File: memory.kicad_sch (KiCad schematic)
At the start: 4 parts

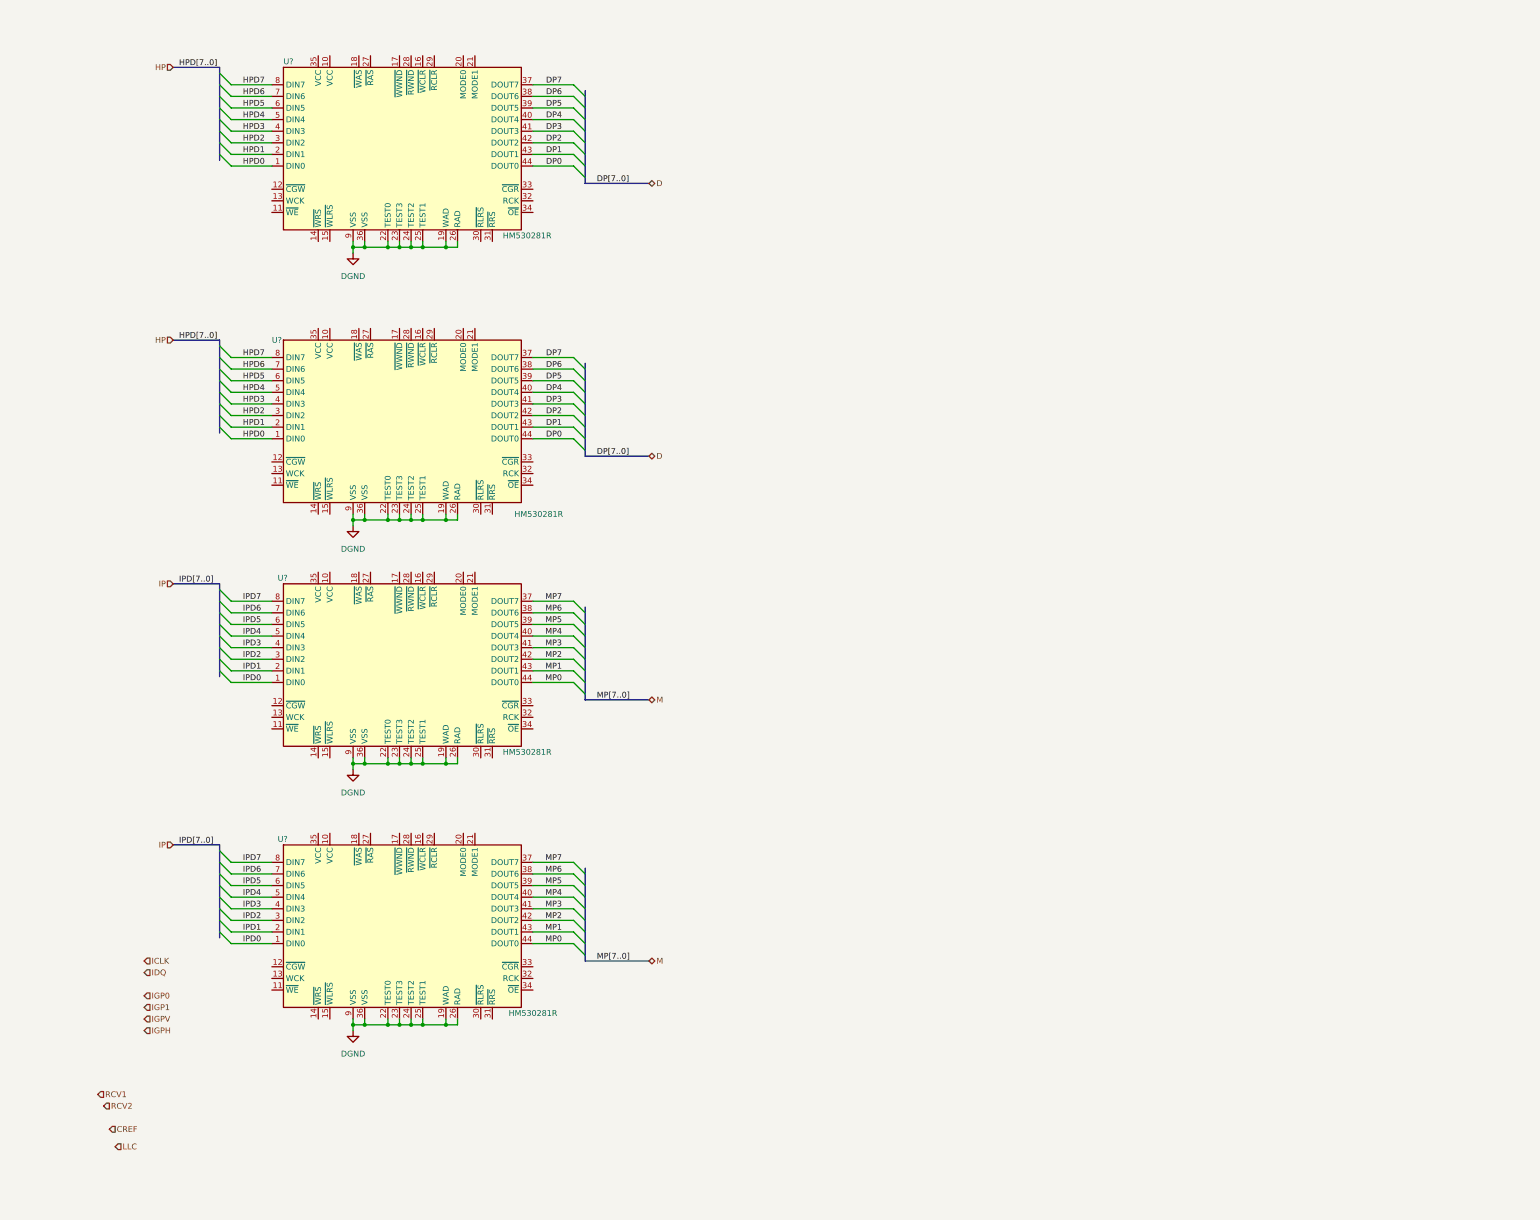
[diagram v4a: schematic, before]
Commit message: continued on schematic, added power sheet
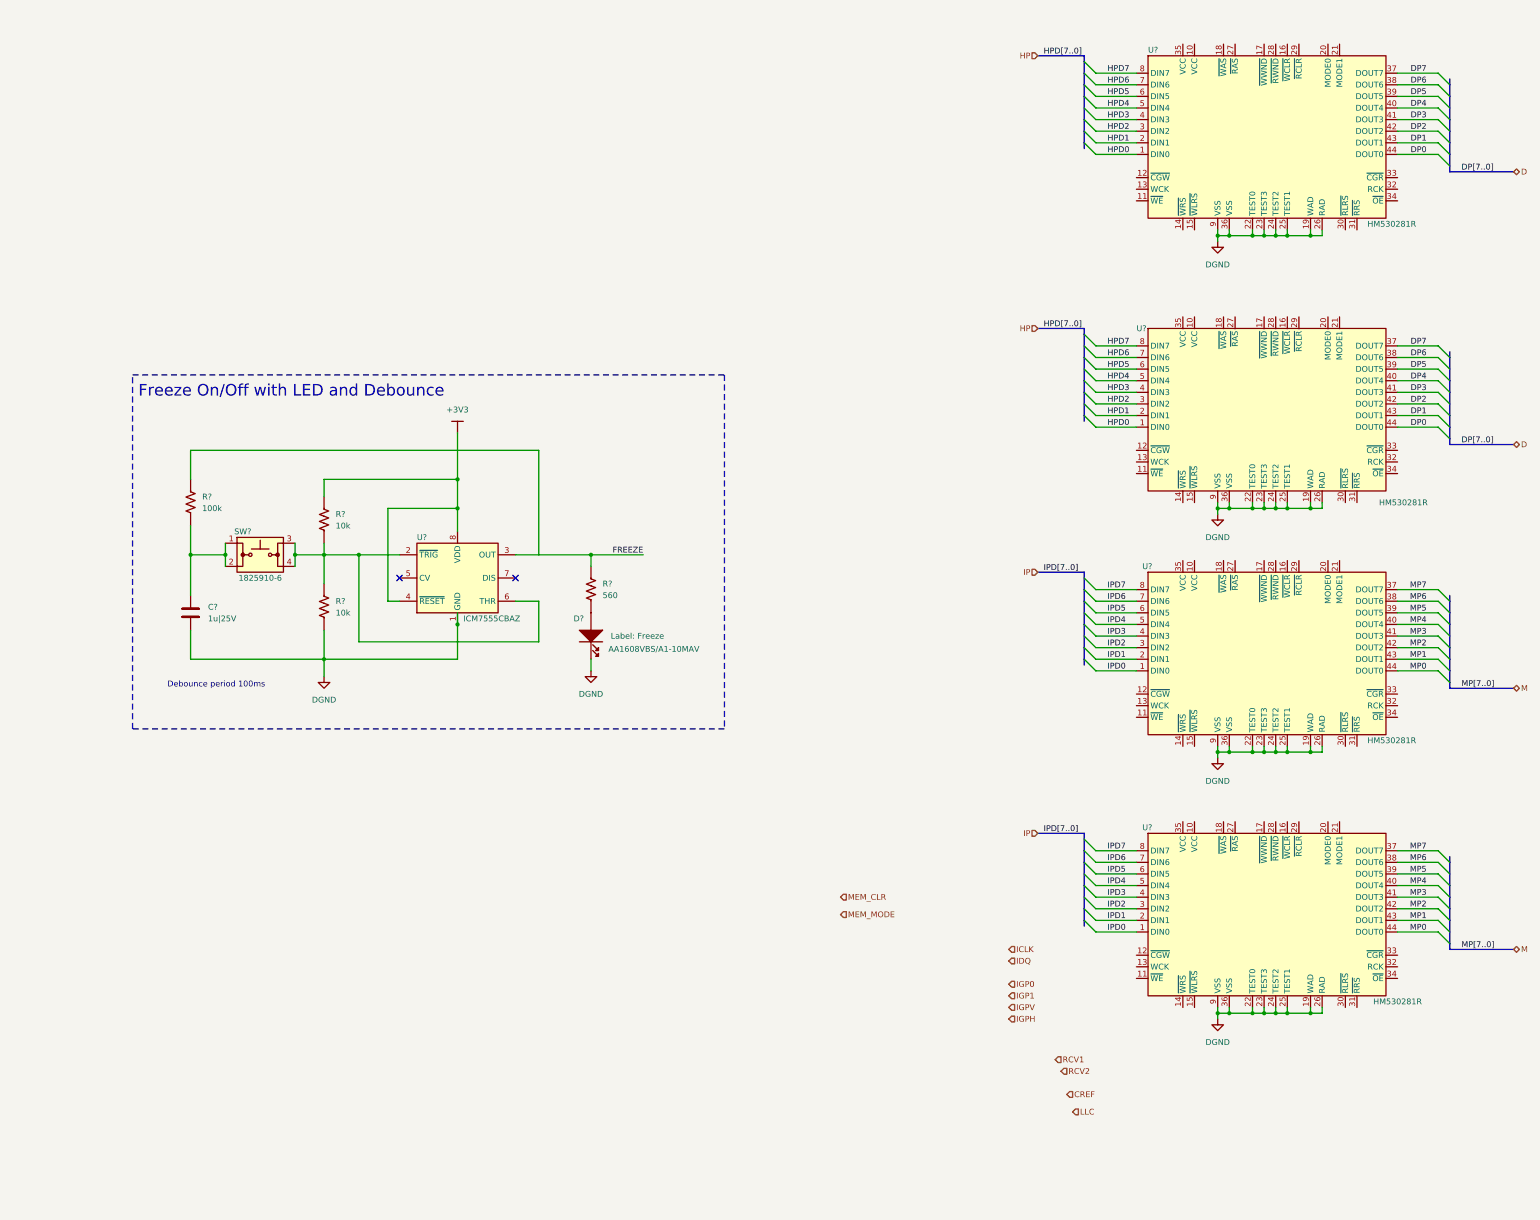
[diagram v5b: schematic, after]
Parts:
- added C?: 1u|25V, symbol tbc:GCJ188R71E105KA01D
- added D?: AA1608VBS/A1-10MAV, symbol tbc:AA1608VBS/A1-10MAV
- added R? (x2): 10k, symbol tbc:RC0603FR-0710KL
- added R?: 560, symbol tbc:RC0603FR-07560RL
- added R?: 100k, symbol tbc:RC0603FR-07100KL
- added SW?: 1825910-6, symbol tbc:1825910-6
- added U?: ICM7555CBAZ, symbol tbc:ICM7555CBAZ
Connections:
- net DGND: now also C?.1, D?.1 (Cathode), R?.1, U?.1 (GND)
- new net: C?.2, R?.1, SW?.1, SW?.2
- new net: R?.1, R?.2, SW?.3, SW?.4, U?.2 (~{TRIG}), U?.6 (THR)
- new net: D?.2 (Anode), R?.1
- new net +3V3: R?.2, U?.4 (~{RESET}), U?.8 (VDD)
- new net FREEZE: R?.2, U?.3 (OUT)
- no-connect marks 0 -> 2
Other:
- note added: "Debounce period 100ms"
- note added: "Freeze On/Off with LED and Debounce"
- moved on the sheet: U?

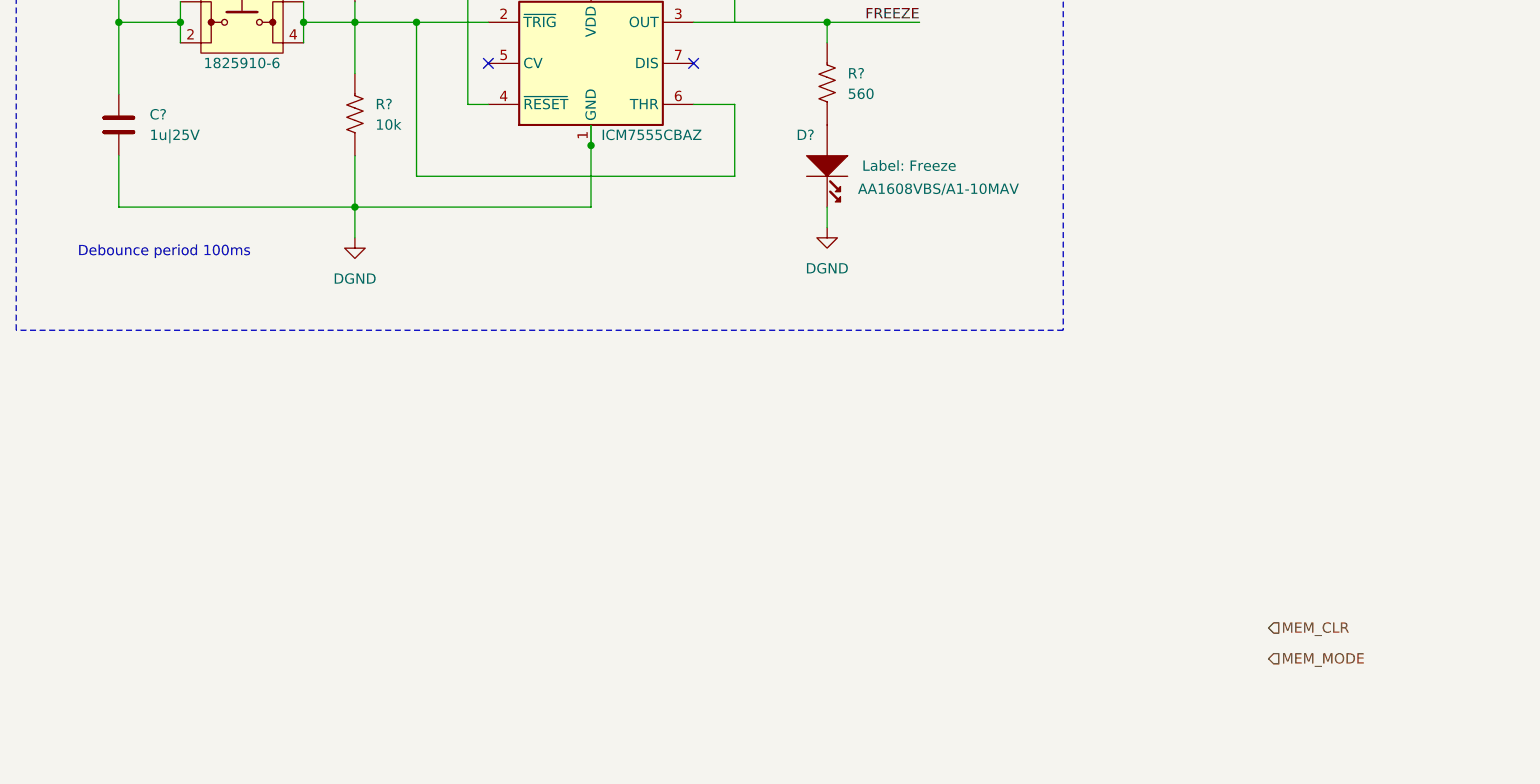
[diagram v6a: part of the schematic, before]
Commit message: added encoder to schematic
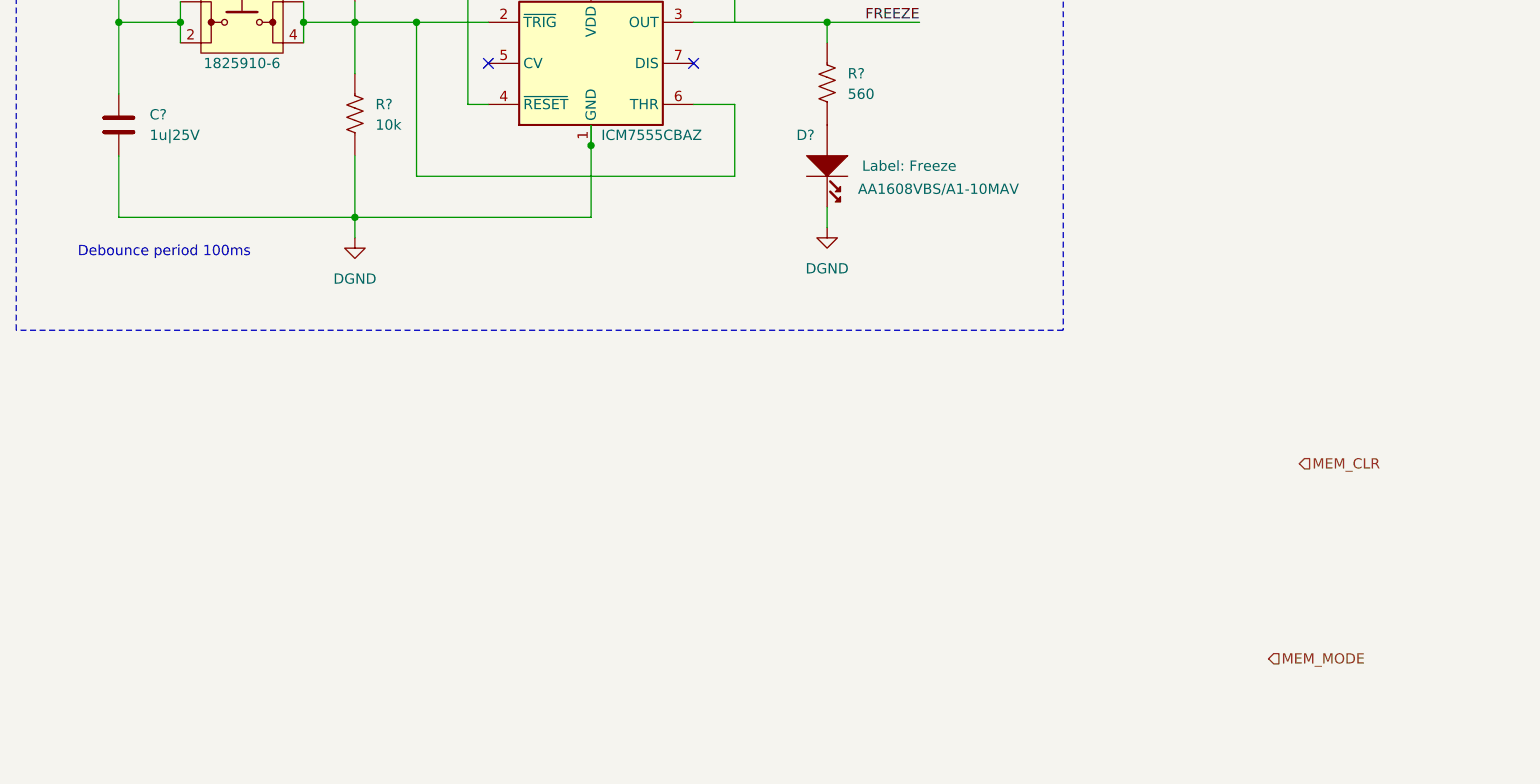
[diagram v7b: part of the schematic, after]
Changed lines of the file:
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@@
   (junction (at 281.94 181.61) (diameter 0) (color 0 0 0 0)
   )
+  (junction (at 83.82 162.56) (diameter 0) (color 0 0 0 0)
+  )
   (junction (at 292.1 238.76) (diameter 0) (color 0 0 0 0)
   )
@@
   )
   (junction (at 289.56 238.76) (diameter 0) (color 0 0 0 0)
-  )
-  (junction (at 83.82 161.29) (diameter 0) (color 0 0 0 0)
   )
   (junction (at 54.61 138.43) (diameter 0) (color 0 0 0 0)
@@
     (stroke (width 0) (type default))
   )
-  (wire (pts (xy 83.82 161.29) (xy 54.61 161.29))
+  (wire (pts (xy 83.82 162.56) (xy 54.61 162.56))
     (stroke (width 0) (type default))
   )
@@
     (stroke (width 0) (type default))
   )
-  (wire (pts (xy 113.03 153.67) (xy 113.03 161.29))
+  (wire (pts (xy 113.03 153.67) (xy 113.03 162.56))
     (stroke (width 0) (type default))
   )
@@
     (stroke (width 0) (type default))
   )
-  (wire (pts (xy 54.61 154.94) (xy 54.61 161.29))
+  (wire (pts (xy 54.61 154.94) (xy 54.61 162.56))
     (stroke (width 0) (type default))
   )
@@
     (stroke (width 0) (type default))
   )
-  (wire (pts (xy 83.82 161.29) (xy 83.82 165.1))
-    (stroke (width 0) (type default))
-  )
   (wire (pts (xy 289.56 68.58) (xy 292.1 68.58))
     (stroke (width 0) (type default))
@@
     (stroke (width 0) (type default))
   )
-  (wire (pts (xy 83.82 161.29) (xy 113.03 161.29))
+  (wire (pts (xy 83.82 162.56) (xy 113.03 162.56))
     (stroke (width 0) (type default))
   )
@@
     (stroke (width 0) (type default))
   )
+  (wire (pts (xy 83.82 162.56) (xy 83.82 165.1))
+    (stroke (width 0) (type default))
+  )
   (wire (pts (xy 289.56 127) (xy 289.56 128.27))
     (stroke (width 0) (type default))
@@
     (stroke (width 0) (type default))
   )
+  (wire (pts (xy 83.82 154.94) (xy 83.82 162.56))
+    (stroke (width 0) (type default))
+  )
   (bus (pts (xy 250.19 199.39) (xy 250.19 200.66))
     (stroke (width 0) (type default))
@@
   )
   (wire (pts (xy 130.81 115.57) (xy 54.61 115.57))
-    (stroke (width 0) (type default))
-  )
-  (wire (pts (xy 83.82 154.94) (xy 83.82 161.29))
     (stroke (width 0) (type default))
   )
@@
     (effects (font (size 1.27 1.27)) (justify right bottom))
   )
-  (hierarchical_label "MEM_CLR" (shape input) (at 196.85 213.36 0) (fields_autoplaced)
+  (hierarchical_label "MEM_CLR" (shape input) (at 200.66 193.04 0) (fields_autoplaced)
     (effects (font (size 1.27 1.27)) (justify left))
   )

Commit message: major progress with memory interfacing
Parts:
- removed C?: 1u|25V, symbol tbc:GCJ188R71E105KA01D
- removed D?: AA1608VBS/A1-10MAV, symbol tbc:AA1608VBS/A1-10MAV
- removed R? (x2): 10k, symbol tbc:RC0603FR-0710KL
- removed R?: 560, symbol tbc:RC0603FR-07560RL
- removed R?: 100k, symbol tbc:RC0603FR-07100KL
- removed SW?: 1825910-6, symbol tbc:1825910-6
- removed U?: ICM7555CBAZ, symbol tbc:ICM7555CBAZ
- added C? (x5): 100n, symbol tbc:GCJ188R71H104KA12D
- added R?: 2K2, symbol tbc:RC0603FR-072K2L
- added R?: 10k, symbol tbc:RC0603FR-0710KL
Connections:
- net DGND is gone; now on net GND: U?.19 (WAD), U?.19 (WAD), U?.19 (WAD), U?.19 (WAD), U?.22 (TEST0), U?.22 (TEST0), U?.22 (TEST0), U?.22 (TEST0), U?.23 (TEST3), U?.23 (TEST3), U?.23 (TEST3), U?.23 (TEST3), U?.24 (TEST2), U?.24 (TEST2), U?.24 (TEST2), U?.24 (TEST2), U?.25 (TEST1), U?.25 (TEST1), U?.25 (TEST1), U?.25 (TEST1), U?.26 (RAD), U?.26 (RAD), U?.26 (RAD), U?.26 (RAD), U?.36 (VSS), U?.36 (VSS), U?.36 (VSS), U?.36 (VSS), U?.9 (VSS), U?.9 (VSS), U?.9 (VSS), U?.9 (VSS)
- net CREF: now also U?.33 (~{CGR}), U?.33 (~{CGR}), U?.33 (~{CGR}), U?.33 (~{CGR})
- net ICLK: now also U?.13 (WCK), U?.13 (WCK), U?.13 (WCK), U?.13 (WCK)
- net IDQ: now also U?.12 (~{CGW}), U?.12 (~{CGW}), U?.12 (~{CGW}), U?.12 (~{CGW})
- net IGPH: now also U?.15 (~{WLRS}), U?.15 (~{WLRS}), U?.15 (~{WLRS}), U?.15 (~{WLRS})
- net IGPV: now also U?.14 (~{WRS}), U?.14 (~{WRS}), U?.14 (~{WRS}), U?.14 (~{WRS})
- net LLC: now also U?.32 (RCK), U?.32 (RCK), U?.32 (RCK), U?.32 (RCK)
- net MEM_CLR: now also U?.16 (~{WCLR}), U?.16 (~{WCLR}), U?.16 (~{WCLR}), U?.16 (~{WCLR}), U?.29 (~{RCLR}), U?.29 (~{RCLR}), U?.29 (~{RCLR}), U?.29 (~{RCLR}), C?.2, R?.1
- net RCV1: now also U?.31 (~{RRS}), U?.31 (~{RRS}), U?.31 (~{RRS}), U?.31 (~{RRS})
- net RCV2: now also U?.30 (~{RLRS}), U?.30 (~{RLRS}), U?.30 (~{RLRS}), U?.30 (~{RLRS})
- net +5V: now reaches U?.10 (VCC)
- net +5V: now also U?.10 (VCC), U?.10 (VCC), U?.10 (VCC), U?.17 (~{WWND}), U?.17 (~{WWND}), U?.17 (~{WWND}), U?.17 (~{WWND}), U?.18 (~{WAS}), U?.18 (~{WAS}), U?.18 (~{WAS}), U?.18 (~{WAS}), U?.27 (~{RAS}), U?.27 (~{RAS}), U?.27 (~{RAS}), U?.27 (~{RAS}), U?.28 (~{RWND}), U?.28 (~{RWND}), U?.28 (~{RWND}), U?.28 (~{RWND}), U?.35 (VCC), U?.35 (VCC), U?.35 (VCC), U?.35 (VCC), C?.2, C?.2, C?.2, C?.2, R?.2, R?.2
- net GND: now reaches U?.20 (MODE0)
- net GND: now also U?.20 (MODE0), U?.20 (MODE0), U?.20 (MODE0), U?.21 (MODE1), U?.21 (MODE1), U?.21 (MODE1), U?.21 (MODE1), C?.1, C?.1, C?.1, C?.1, C?.1, R?.1
- net Q2: now reaches U?.34 (~{OE})
- net Q2: now also U?.34 (~{OE})
- net Q1: now reaches U?.34 (~{OE})
- net Q1: now also U?.34 (~{OE})
- no-connect marks 2 -> 0
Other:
- note added: "MODE0 Set"
- note added: "POR/Clear"
- note removed: "Debounce period 100ms"
- note removed: "Freeze On/Off with LED and Debounce"
- moved on the sheet: U?
